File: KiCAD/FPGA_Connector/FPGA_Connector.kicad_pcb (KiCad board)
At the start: 2 copper layers, 46.5 x 42.5 mm, 3 parts, among them J1 VGA, J2 Pmod 1, J3 Pmod 2

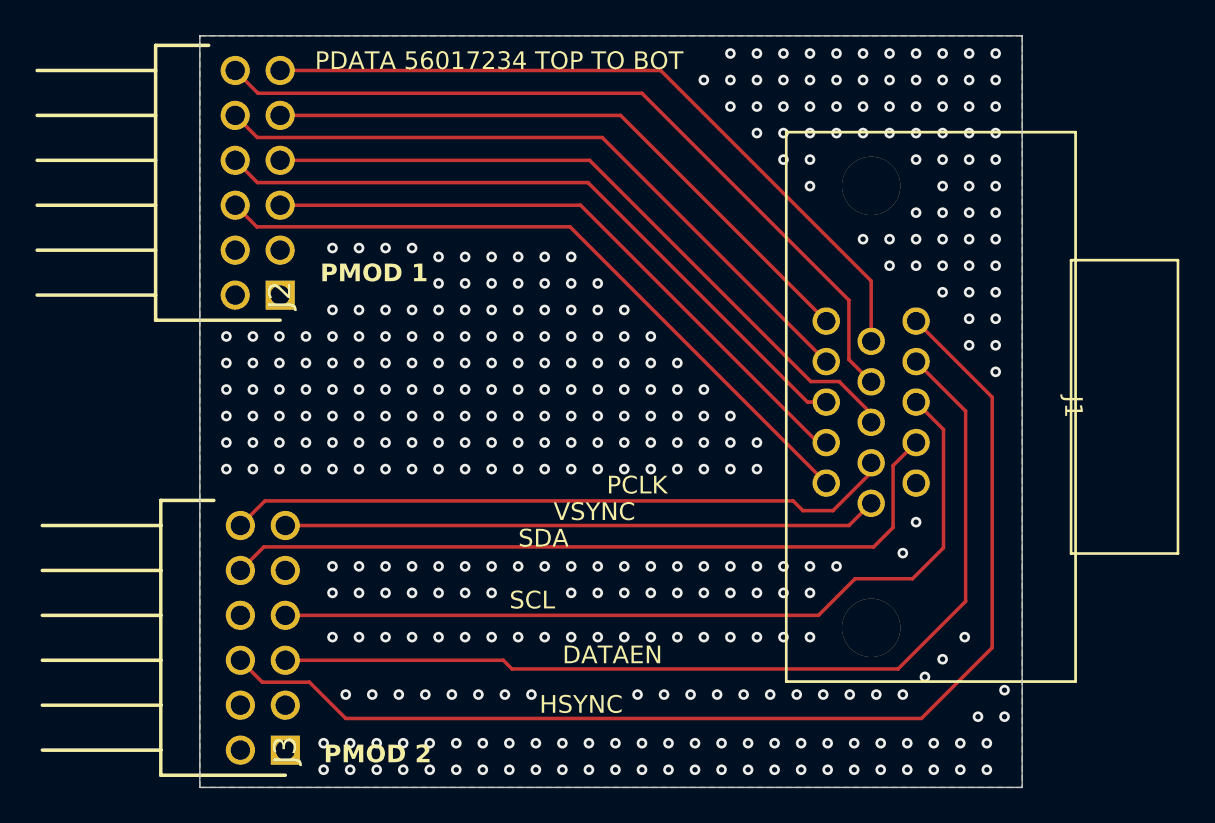
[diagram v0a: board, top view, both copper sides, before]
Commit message: added 3d models to FPGA Board
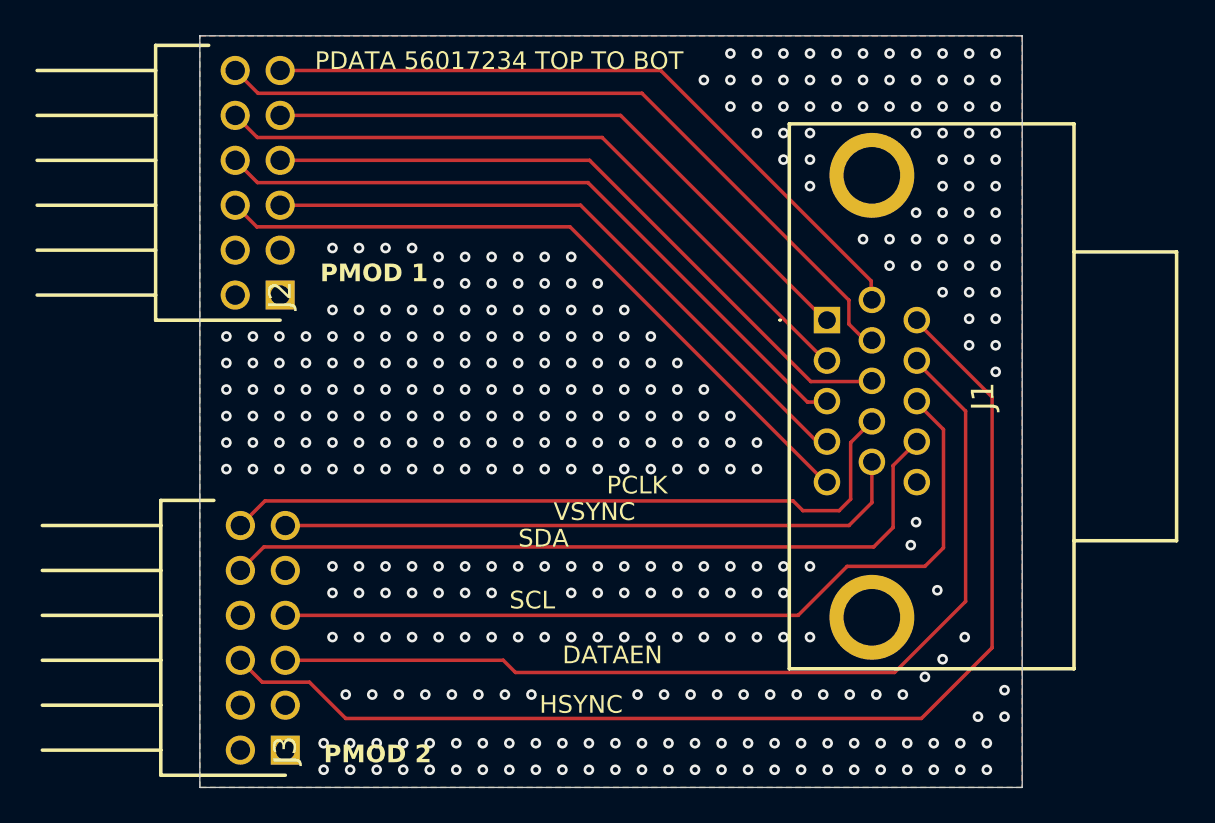
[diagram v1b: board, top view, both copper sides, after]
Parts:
- J1: footprint footprints:CONN_AHDF15A-KG-TAXB_ASM -> footprints:AHDF15AKGTAXB
- moved J1 14.8 mm to (176.5, 90.1), turned to 90 degrees
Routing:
- net /PCLK: track 38.0 -> 40.5 mm
- net /VSYNC: track 33.6 -> 36.0 mm
- net /PDATA6: track 45.2 -> 43.0 mm
- net /PDATA7: track 40.2 -> 38.0 mm
- net /PDATA5: track 41.8 -> 39.8 mm
- net GND: track 0.32 -> 0.00 mm, vias 357 -> 352
